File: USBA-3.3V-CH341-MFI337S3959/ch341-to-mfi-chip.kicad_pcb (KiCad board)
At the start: 2 copper layers, 23.5 x 18.4 mm, 15 parts, among them J1 USB-212-BCW, U1 CH341F, U2 HR1117V-3.3, U3 MFI337S3959

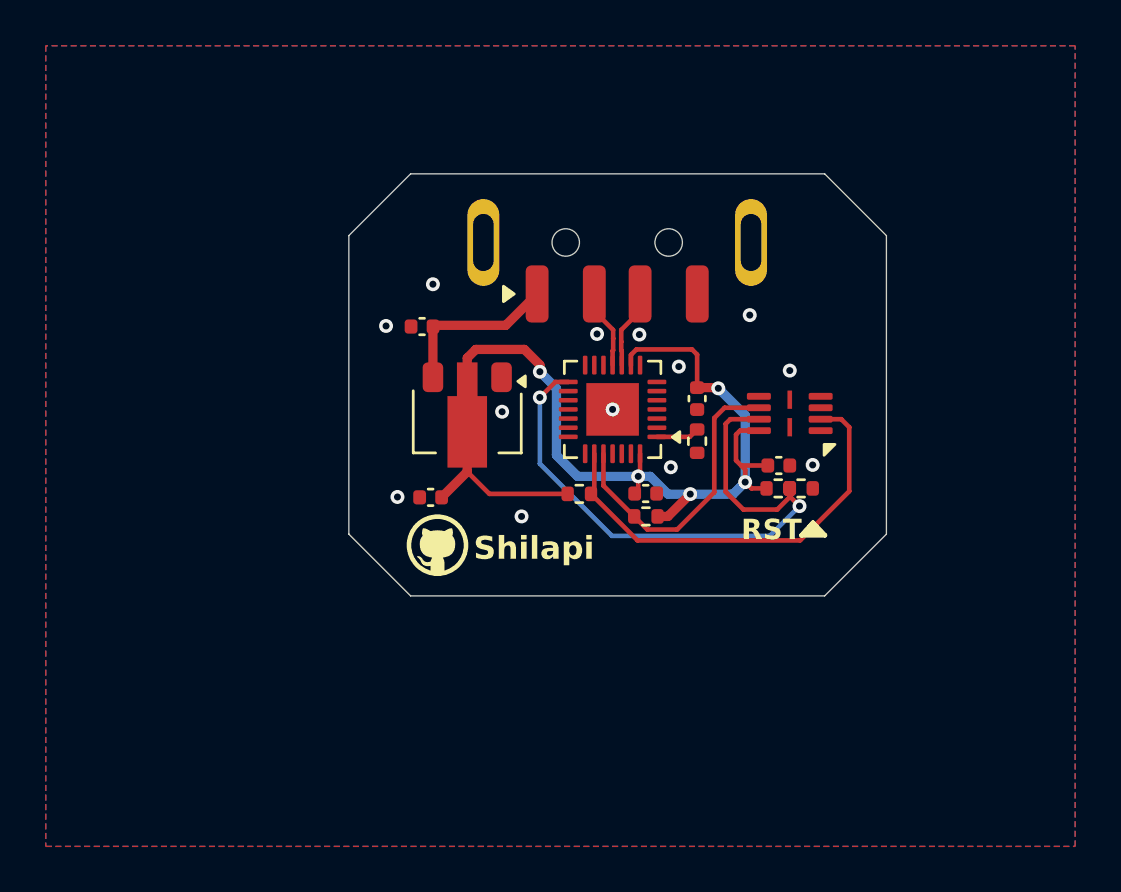
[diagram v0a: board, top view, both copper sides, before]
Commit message: add tiny layout of the dongle
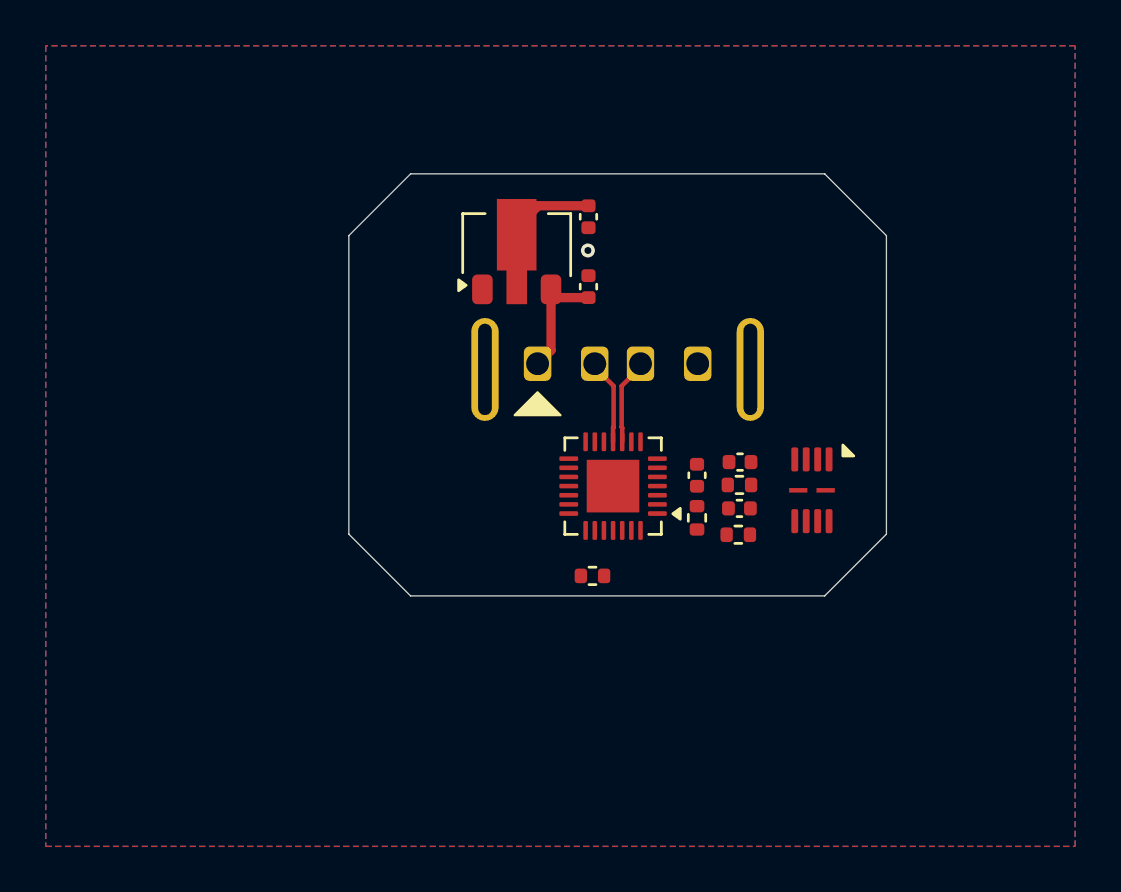
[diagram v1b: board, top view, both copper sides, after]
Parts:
- removed R5: 4.7k, Resistor_SMD:R_0402_1005Metric
- G***: moved to B.Cu
- J1: footprint Connector_USB:USB_A_Connfly_DS1098_Horizontal -> footprint:917-511A1015B20200
- moved C1 14.1 mm to (73.7, 40.0), turned to -90 degrees
- moved J1 13.6 mm to (75.0, 46.4), turned to 0 degrees
- moved U2 8.04 mm to (70.6, 41.2), turned to 90 degrees
- moved C2 7.48 mm to (73.7, 43.0), turned to 90 degrees
- moved G*** 6.10 mm to (73.2, 54.4), turned to 180 degrees
- moved C3 4.15 mm to (80.3, 52.7)
- moved R3 4.12 mm to (80.3, 53.9)
- moved R2 3.63 mm to (73.9, 55.7), turned to 180 degrees
- moved U3 3.49 mm to (83.5, 51.9), turned to -90 degrees
- moved U1 3.35 mm to (74.8, 51.8)
- moved C5 3.35 mm to (78.5, 51.3)
- moved R1 3.35 mm to (78.5, 53.1)
- moved C4 1.70 mm to (80.3, 50.7)
- moved R4 1.70 mm to (80.3, 51.7)
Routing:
- net +3V3: track 48.2 -> 6.15 mm, vias 5 -> 0
- net Net-(U1-CS0): track 26.8 -> 0.00 mm, vias 2 -> 0
- net Net-(U1-SDA): track 19.0 -> 0.00 mm
- net Net-(U1-SCL): track 13.1 -> 0.00 mm
- net Net-(J1-VBUS): track 7.39 -> 5.28 mm
- net Net-(U1-ACT#): track 1.89 -> 0.00 mm
- net GND: vias 13 -> 1
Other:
- board text removed: "RST"
